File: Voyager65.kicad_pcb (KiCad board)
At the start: 2 copper layers, 303.2 x 94.5 mm, 225 parts, among them P1 TC2030-IDC, SW1 SW_PUSH, U1 ATXMEGA32A4U-AU, U2 MCP1700T-3002E/TT, U3 PRTR5V0U2X, U4 IS31FL3733, U5 74LVC1G34

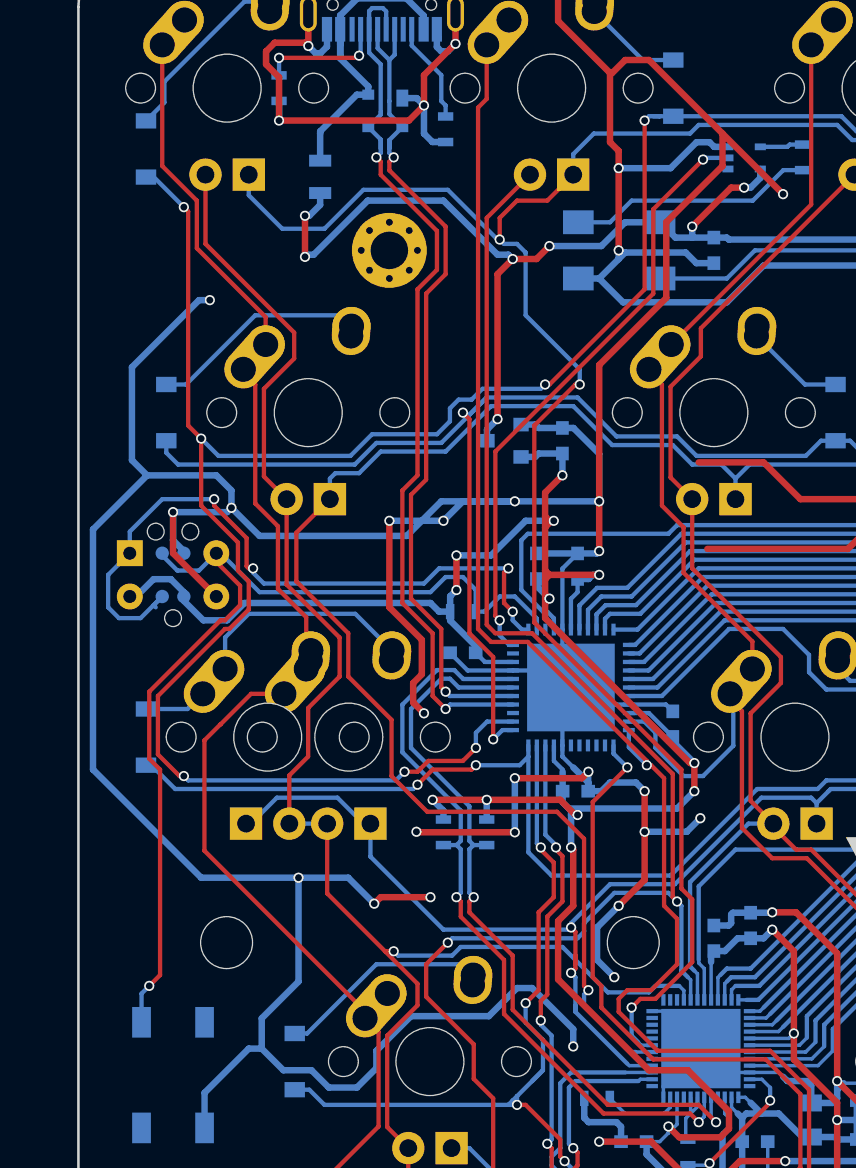
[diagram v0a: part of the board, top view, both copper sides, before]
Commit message: Tune top plate
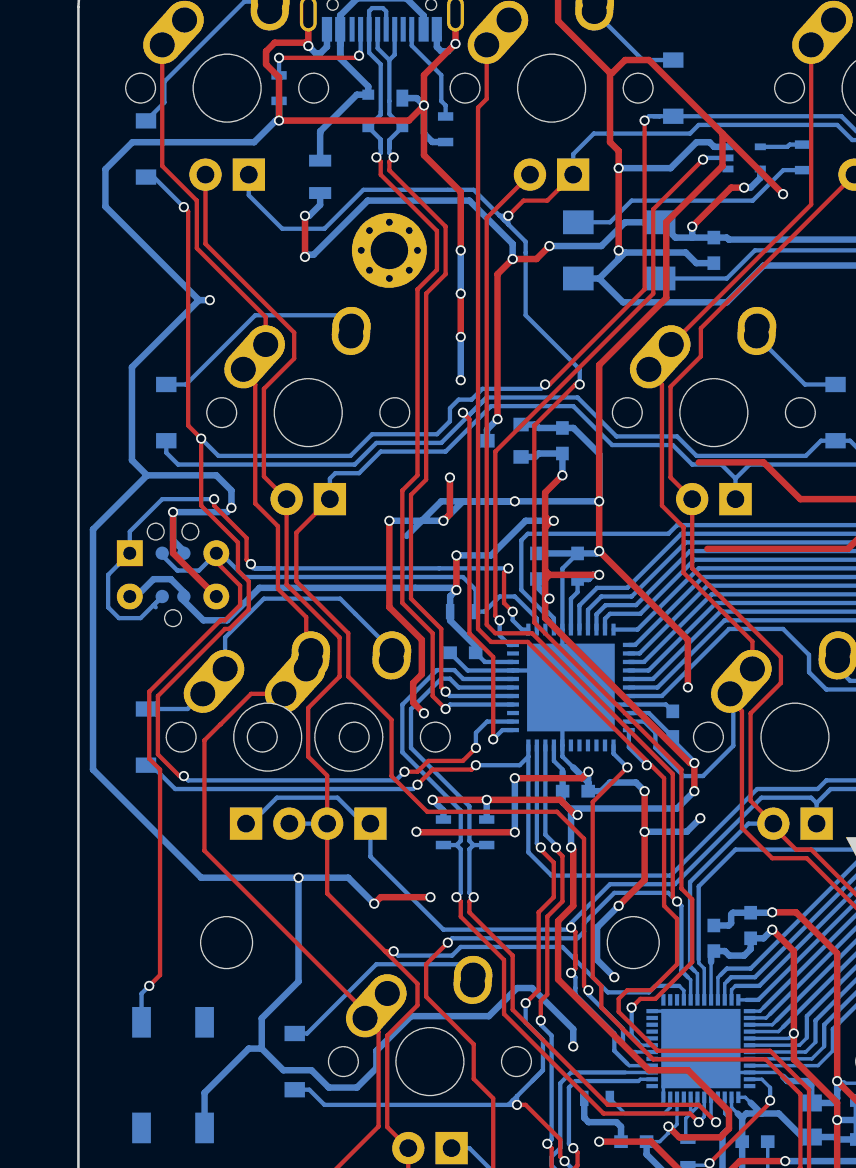
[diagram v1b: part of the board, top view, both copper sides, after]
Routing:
- net GND: track 2165.3 -> 2205.5 mm, vias 85 -> 91
- net +5V: track 722.7 -> 723.8 mm
- net PDI_CLK: track 58.6 -> 57.8 mm
- net Net-(D30-Pad2): track 16.8 -> 17.6 mm
- net +3V3: track 147.3 -> 147.8 mm

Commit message: Generate first set of gerbers
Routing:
- net GND: track 2205.5 -> 2200.2 mm, vias 91 -> 92
- net Net-(LED4-Pad2): track 73.4 -> 71.5 mm
- net +5V: track 723.8 -> 722.4 mm

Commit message: Prepare gerbers for production
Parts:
- USB1: value HRO-TYPE-C-31-M-12 -> Wurth-632723300011; footprint Type-C:HRO-TYPE-C-31-M-12 -> Type-C:Wurth-632723300011-MaximumExtensionMount
- moved U3 1.59 mm to (66.4, 60.1), turned to 90 degrees
- moved USB1 0.80 mm to (66.2, 45.2)
- moved R7 0.18 mm to (70.1, 59.7), turned to 90 degrees
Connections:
- USB1 pad 10: Net-(R7-Pad1) -> Net-(USB1-Pad10)
- USB1 pad 11: VCC -> Net-(USB1-Pad11)
- USB1 pad 2: VCC -> Net-(USB1-Pad2)
- USB1 pad 4: Net-(R6-Pad2) -> VCC
- USB1 pad 5: D- -> Net-(R6-Pad2)
- USB1 pad 8: D+ -> Net-(USB1-Pad8)
- USB1 pad 9: Net-(USB1-Pad9) -> VCC
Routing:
- net Net-(R7-Pad1): track 5.94 -> 20.9 mm, vias 0 -> 1
- net D+: track 49.6 -> 53.6 mm, vias 2 -> 3
- net Net-(R6-Pad2): track 7.37 -> 10.8 mm
- net VCC: track 21.9 -> 24.6 mm, vias 0 -> 4
- net GND: track 2200.2 -> 2202.7 mm, vias 92 -> 91
- net D-: track 52.1 -> 49.9 mm, vias 2 -> 3
- net Net-(D64-Pad2): track 24.1 -> 24.9 mm

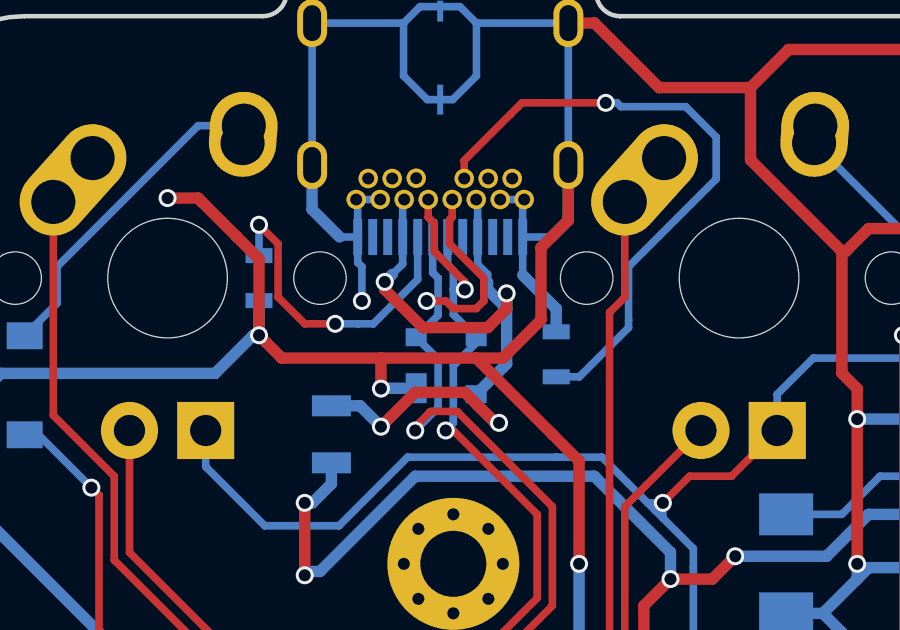
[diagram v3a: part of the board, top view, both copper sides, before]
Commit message: Tune USB connector
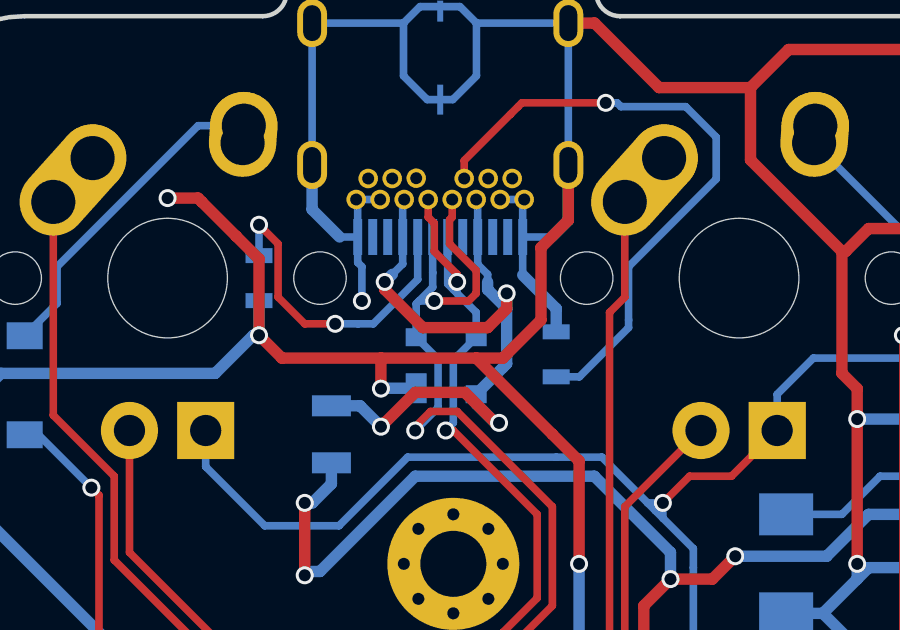
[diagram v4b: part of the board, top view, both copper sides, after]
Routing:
- net D+: track 53.6 -> 52.6 mm
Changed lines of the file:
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@@
     (thickness 1.6)
     (drawings 79)
-    (tracks 3672)
+    (tracks 3666)
     (zones 0)
     (modules 225)
@@
   (segment (start 52.451 62.435375) (end 52.3875 62.371875) (width 0.254) (layer B.Cu) (net 25) (status 30))
   (via (at 55.626 77.724) (size 0.6) (drill 0.4) (layers F.Cu B.Cu) (net 25))
+  (segment (start 66.421 62.23) (end 66.675 61.976) (width 0.254) (layer B.Cu) (net 27))
+  (segment (start 66.675 61.976) (end 66.675 59.883) (width 0.254) (layer B.Cu) (net 27))
+  (segment (start 66.675 59.883) (end 67.437 59.121) (width 0.254) (layer B.Cu) (net 27))
+  (segment (start 66.802 57.277) (end 66.802 57.023) (width 0.254) (layer F.Cu) (net 27))
+  (segment (start 66.802 57.023) (end 66.04 56.261) (width 0.254) (layer F.Cu) (net 27))
+  (segment (start 66.04 56.261) (end 66.04 55.3204) (width 0.254) (layer F.Cu) (net 27))
+  (segment (start 66.04 55.3204) (end 65.8376 55.118) (width 0.254) (layer F.Cu) (net 27))
+  (segment (start 65.8376 55.118) (end 65.8376 54.53) (width 0.254) (layer F.Cu) (net 27))
+  (segment (start 67.437 58.293) (end 66.802 57.658) (width 0.254) (layer B.Cu) (net 27))
+  (segment (start 66.802 57.658) (end 66.675 57.531) (width 0.254) (layer B.Cu) (net 27))
+  (segment (start 66.802 57.277) (end 66.802 57.658) (width 0.254) (layer B.Cu) (net 27))
+  (via (at 66.802 57.277) (size 0.6) (drill 0.4) (layers F.Cu B.Cu) (net 27))
+  (segment (start 66.4876 55.78) (end 66.4876 57.3436) (width 0.254) (layer B.Cu) (net 27))
+  (segment (start 66.4876 57.3436) (end 66.675 57.531) (width 0.254) (layer B.Cu) (net 27))
+  (segment (start 67.437 59.121) (end 67.437 58.293) (width 0.254) (layer B.Cu) (net 27))
   (segment (start 69.977 93.599) (end 69.215 92.837) (width 0.254) (layer F.Cu) (net 27))
   (segment (start 69.215 92.837) (end 69.215 89.154) (width 0.254) (layer F.Cu) (net 27))
@@
   (segment (start 68.326 68.961) (end 69.469 67.818) (width 0.254) (layer F.Cu) (net 27))
   (segment (start 66.675 62.23) (end 66.421 62.23) (width 0.254) (layer F.Cu) (net 27))
-  (segment (start 67.056 57.277) (end 66.04 56.261) (width 0.254) (layer F.Cu) (net 27))
-  (segment (start 65.8376 54.53) (end 65.8376 55.118) (width 0.254) (layer F.Cu) (net 27))
-  (segment (start 66.04 56.261) (end 66.04 55.3204) (width 0.254) (layer F.Cu) (net 27))
-  (segment (start 66.04 55.3204) (end 65.8376 55.118) (width 0.254) (layer F.Cu) (net 27))
-  (segment (start 67.056 57.531) (end 67.056 57.277) (width 0.254) (layer F.Cu) (net 27))
-  (segment (start 66.675 56.896) (end 66.675 57.531) (width 0.254) (layer B.Cu) (net 27))
-  (segment (start 66.675 57.531) (end 66.675 58.039) (width 0.254) (layer B.Cu) (net 27))
-  (segment (start 67.056 57.531) (end 66.675 57.531) (width 0.254) (layer B.Cu) (net 27))
-  (via (at 67.056 57.531) (size 0.6) (drill 0.4) (layers F.Cu B.Cu) (net 27))
-  (segment (start 66.675 58.039) (end 66.675 58.359) (width 0.254) (layer B.Cu) (net 27))
-  (segment (start 66.675 61.849) (end 66.675 61.976) (width 0.254) (layer B.Cu) (net 27))
-  (segment (start 66.675 61.976) (end 66.421 62.23) (width 0.254) (layer B.Cu) (net 27))
   (via (at 66.421 62.23) (size 0.6) (drill 0.4) (layers F.Cu B.Cu) (net 27))
-  (segment (start 66.675 61.722) (end 66.675 61.849) (width 0.254) (layer B.Cu) (net 27))
-  (segment (start 66.675 60.071) (end 66.675 61.722) (width 0.254) (layer B.Cu) (net 27))
-  (segment (start 67.437 59.309) (end 66.675 60.071) (width 0.254) (layer B.Cu) (net 27))
-  (segment (start 67.437 59.121) (end 67.437 59.309) (width 0.254) (layer B.Cu) (net 27))
-  (segment (start 66.675 58.359) (end 67.437 59.121) (width 0.254) (layer B.Cu) (net 27))
-  (segment (start 66.4876 56.7086) (end 66.675 56.896) (width 0.254) (layer B.Cu) (net 27))
-  (segment (start 66.4876 55.78) (end 66.4876 56.7086) (width 0.254) (layer B.Cu) (net 27))
   (segment (start 69.977 93.599) (end 70.23825 93.33775) (width 0.254) (layer B.Cu) (net 27))
   (via (at 69.977 93.599) (size 0.6) (drill 0.4) (layers F.Cu B.Cu) (net 27))
   (segment (start 73.93425 93.33775) (end 70.23825 93.33775) (width 0.254) (layer B.Cu) (net 27) (status 10))
+  (segment (start 65.9876 57.4564) (end 65.532 57.912) (width 0.254) (layer B.Cu) (net 28))
+  (segment (start 65.532 57.912) (end 65.437 58.007) (width 0.254) (layer B.Cu) (net 28))
+  (segment (start 66.04 57.912) (end 65.532 57.912) (width 0.254) (layer B.Cu) (net 28))
+  (segment (start 67.183 57.912) (end 66.04 57.912) (width 0.254) (layer F.Cu) (net 28))
+  (via (at 66.04 57.912) (size 0.6) (drill 0.4) (layers F.Cu B.Cu) (net 28))
+  (segment (start 67.437 57.658) (end 67.183 57.912) (width 0.254) (layer F.Cu) (net 28))
+  (segment (start 67.437 56.896) (end 66.548 56.007) (width 0.254) (layer F.Cu) (net 28))
+  (segment (start 67.437 56.896) (end 67.437 57.658) (width 0.254) (layer F.Cu) (net 28))
+  (segment (start 65.437 58.007) (end 65.437 59.121) (width 0.254) (layer B.Cu) (net 28))
+  (segment (start 65.9876 56.9706) (end 65.9876 57.4564) (width 0.254) (layer B.Cu) (net 28))
   (segment (start 65.405 62.23) (end 65.405 62.103) (width 0.254) (layer F.Cu) (net 28))
   (segment (start 67.945 81.026) (end 67.945 87.122) (width 0.254) (layer F.Cu) (net 28))
@@
   (segment (start 69.977 68.072) (end 68.834 69.215) (width 0.254) (layer F.Cu) (net 28))
   (segment (start 69.723 92.329) (end 69.977 92.583) (width 0.254) (layer F.Cu) (net 28))
-  (segment (start 65.786 57.912) (end 66.421 57.912) (width 0.254) (layer F.Cu) (net 28))
-  (segment (start 66.421 57.912) (end 66.675 58.166) (width 0.254) (layer F.Cu) (net 28))
-  (segment (start 66.675 58.166) (end 67.437 58.166) (width 0.254) (layer F.Cu) (net 28))
-  (segment (start 67.437 58.166) (end 67.691 57.912) (width 0.254) (layer F.Cu) (net 28))
-  (segment (start 67.691 57.912) (end 67.691 57.15) (width 0.254) (layer F.Cu) (net 28))
-  (segment (start 67.691 57.15) (end 66.548 56.007) (width 0.254) (layer F.Cu) (net 28))
   (segment (start 66.548 56.007) (end 66.548 55.2076) (width 0.254) (layer F.Cu) (net 28))
   (segment (start 66.548 55.2076) (end 66.6376 55.118) (width 0.254) (layer F.Cu) (net 28))
   (segment (start 66.6376 55.118) (end 66.6376 54.53) (width 0.254) (layer F.Cu) (net 28))
-  (segment (start 66.167 57.15) (end 66.167 57.912) (width 0.254) (layer B.Cu) (net 28))
-  (segment (start 65.786 57.912) (end 66.167 57.912) (width 0.254) (layer B.Cu) (net 28))
-  (segment (start 66.167 57.912) (end 66.167 58.391) (width 0.254) (layer B.Cu) (net 28))
-  (via (at 65.786 57.912) (size 0.6) (drill 0.4) (layers F.Cu B.Cu) (net 28))
   (segment (start 66.167 61.468) (end 66.167 59.851) (width 0.254) (layer B.Cu) (net 28))
   (segment (start 66.167 61.468) (end 65.405 62.23) (width 0.254) (layer B.Cu) (net 28))
   (via (at 65.405 62.23) (size 0.6) (drill 0.4) (layers F.Cu B.Cu) (net 28))
   (segment (start 66.167 59.851) (end 65.437 59.121) (width 0.254) (layer B.Cu) (net 28))
-  (segment (start 66.167 58.391) (end 65.437 59.121) (width 0.254) (layer B.Cu) (net 28))
-  (segment (start 65.9876 56.9706) (end 66.167 57.15) (width 0.254) (layer B.Cu) (net 28))
   (segment (start 65.9876 55.78) (end 65.9876 56.9706) (width 0.254) (layer B.Cu) (net 28))
   (segment (start 70.23175 92.83775) (end 69.977 92.583) (width 0.254) (layer B.Cu) (net 28))
